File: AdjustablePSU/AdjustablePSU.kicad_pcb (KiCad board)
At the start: 2 copper layers, 99.1 x 96.5 mm, 38 parts

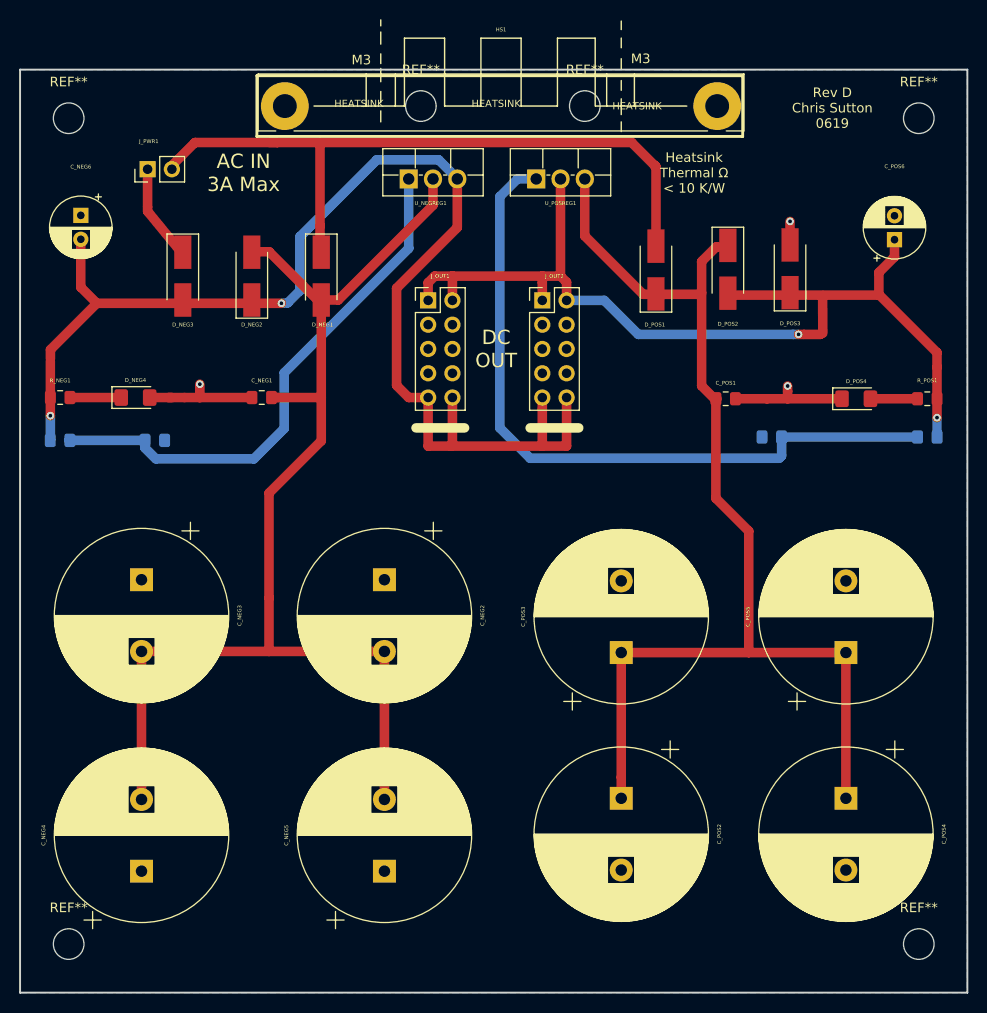
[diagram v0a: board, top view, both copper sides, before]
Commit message: Adjustable PSU RevD
- Layout Redesign 97mm x 50mm
- Removed 4/8 Large Electrolytic Caps
- Added Power Resistor pair to filter ripple.
- Added docs: Layer SVG, Schema SVG/PDF, PNG Renders, STEP 3D model
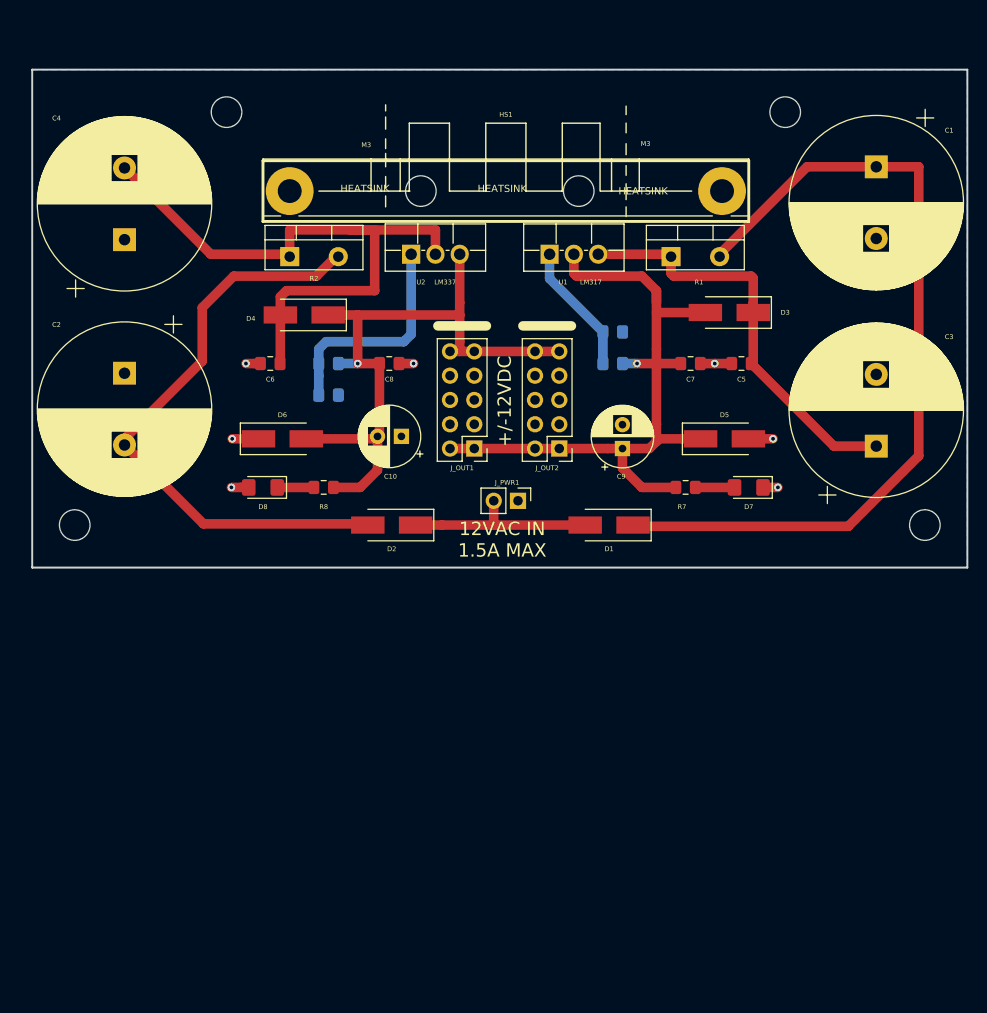
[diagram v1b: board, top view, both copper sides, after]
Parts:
- removed C_NEG1, C_POS1: 100nF, Capacitor_SMD:C_0805_2012Metric_Pad1.15x1.40mm_HandSolder
- removed C_NEG2, C_NEG3, C_NEG4, C_NEG5, C_POS2, C_POS3, C_POS4, C_POS5: 3300uF, Capacitor_THT:CP_Radial_D18.0mm_P7.50mm
- removed C_NEG6, C_POS6: 100uF, Capacitor_THT:CP_Radial_D6.3mm_P2.50mm
- removed D_NEG1, D_NEG2, D_NEG3, D_POS1, D_POS2, D_POS3: HER202G, Diode_SMD:D_SMA_Handsoldering
- removed D_NEG4, D_POS4: LED, LED_SMD:LED_1206_3216Metric_Pad1.42x1.75mm_HandSolder
- removed R_NEG1, R_POS1: 1K, Resistor_SMD:R_0805_2012Metric_Pad1.15x1.40mm_HandSolder
- removed R_NEGREG1, R_POSREG1: 120R, Resistor_SMD:R_0805_2012Metric_Pad1.15x1.40mm_HandSolder
- removed R_NEGREG2, R_POSREG2: 1K1, Resistor_SMD:R_0805_2012Metric_Pad1.15x1.40mm_HandSolder
- removed U_NEGREG1: LM337_TO220, Package_TO_SOT_THT:TO-220F-3_Vertical
- removed U_POSREG1: LM317_3PinPackage, Package_TO_SOT_THT:TO-220F-3_Vertical
- added C1: 3300uF, Capacitor_THT:CP_Radial_D18.0mm_P7.50mm, F.Cu at (188.6, 66.0)
- added C10: 10uF, Capacitor_THT:CP_Radial_D6.3mm_P2.50mm, F.Cu at (138.9, 94.2)
- added C2: 3300uF, Capacitor_THT:CP_Radial_D18.0mm_P7.50mm, F.Cu at (110.0, 87.6)
- added C3: 3300uF, Capacitor_THT:CP_Radial_D18.0mm_P7.50mm, F.Cu at (188.6, 95.2)
- added C4: 3300uF, Capacitor_THT:CP_Radial_D18.0mm_P7.50mm, F.Cu at (110.0, 73.7)
- added C5: 100nF, Capacitor_SMD:C_0805_2012Metric_Pad1.15x1.40mm_HandSolder, F.Cu at (174.5, 86.6)
- added C6: 100nF, Capacitor_SMD:C_0805_2012Metric_Pad1.15x1.40mm_HandSolder, F.Cu at (125.2, 86.6)
- added C7: 100nF, Capacitor_SMD:C_0805_2012Metric_Pad1.15x1.40mm_HandSolder, F.Cu at (169.2, 86.6)
- added C8: 100nF, Capacitor_SMD:C_0805_2012Metric_Pad1.15x1.40mm_HandSolder, F.Cu at (137.7, 86.6)
- added C9: 10uF, Capacitor_THT:CP_Radial_D6.3mm_P2.50mm, F.Cu at (162.1, 95.5)
- added D1: HER202G, Diode_SMD:D_SMA_Handsoldering, F.Cu at (160.7, 103.5)
- added D2: HER202G, Diode_SMD:D_SMA_Handsoldering, F.Cu at (137.9, 103.5)
- added D3: HER202G, Diode_SMD:D_SMA_Handsoldering, F.Cu at (173.2, 81.3)
- added D4: HER202G, Diode_SMD:D_SMA_Handsoldering, F.Cu at (128.8, 81.5)
- added D5: HER202G, Diode_SMD:D_SMA_Handsoldering, F.Cu at (172.7, 94.5)
- added D6: HER202G, Diode_SMD:D_SMA_Handsoldering, F.Cu at (126.5, 94.5)
- added D7: LED, LED_SMD:LED_1206_3216Metric_Pad1.42x1.75mm_HandSolder, F.Cu at (175.3, 99.6)
- added D8: LED, LED_SMD:LED_1206_3216Metric_Pad1.42x1.75mm_HandSolder, F.Cu at (124.5, 99.6)
- added R1: R, Package_TO_SOT_THT:TO-220-2_Vertical, F.Cu at (167.1, 75.4)
- added R2: R, Package_TO_SOT_THT:TO-220-2_Vertical, F.Cu at (127.3, 75.4)
- added R3: 120R, Resistor_SMD:R_0805_2012Metric_Pad1.15x1.40mm_HandSolder, B.Cu at (161.0, 86.6)
- added R4: 1K1, Resistor_SMD:R_0805_2012Metric_Pad1.15x1.40mm_HandSolder, B.Cu at (161.0, 83.3)
- added R5: 120R, Resistor_SMD:R_0805_2012Metric_Pad1.15x1.40mm_HandSolder, B.Cu at (131.3, 86.6)
- added R6: 1K1, Resistor_SMD:R_0805_2012Metric_Pad1.15x1.40mm_HandSolder, B.Cu at (131.3, 89.9)
- added R7: 1K, Resistor_SMD:R_0805_2012Metric_Pad1.15x1.40mm_HandSolder, F.Cu at (168.7, 99.6)
- added R8: 1K, Resistor_SMD:R_0805_2012Metric_Pad1.15x1.40mm_HandSolder, F.Cu at (130.8, 99.6)
- added U1: LM317_3PinPackage, Package_TO_SOT_THT:TO-220F-3_Vertical, F.Cu at (154.4, 75.2)
- added U2: LM337_TO220, Package_TO_SOT_THT:TO-220F-3_Vertical, F.Cu at (140.0, 75.2)
- moved J_PWR1 52.0 mm to (151.1, 101.0), turned to 270 degrees
- moved REF** 43.8 mm to (104.8, 103.5)
- moved REF** 43.8 mm to (193.7, 103.5)
- moved REF** 16.5 mm to (120.7, 60.3)
- moved J_OUT1 16.2 mm to (146.6, 95.5), turned to 180 degrees
- moved J_OUT2 15.6 mm to (155.4, 95.5), turned to 180 degrees
- moved REF** 14.0 mm to (179.1, 60.3)
- moved REF** 8.91 mm to (157.5, 68.6)
- moved HS1 8.90 mm to (149.9, 68.6)
- moved REF** 8.89 mm to (141.0, 68.6)
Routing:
- net Net-(R_POSREG1-Pad2): track 75.8 -> 0.00 mm
- net Net-(C4-Pad2): track 0.00 -> 67.2 mm
- net /12VDC_NEG_REG: track 134.4 -> 69.2 mm, vias 2 -> 1
- net /DC_NEG_IN: track 128.1 -> 64.5 mm
- net Net-(R_NEGREG1-Pad2): track 56.6 -> 0.00 mm
- net /AC_IN: track 74.2 -> 20.3 mm
- net Net-(C3-Pad1): track 0.00 -> 44.8 mm
- net /DC_POS_IN: track 120.9 -> 87.7 mm
- net /12VDC_POS_REG: track 106.0 -> 74.7 mm, vias 2 -> 1
- net Net-(R5-Pad2): track 0.00 -> 23.5 mm
- net GND: track 37.1 -> 15.0 mm, vias 3 -> 7
- net Net-(R3-Pad2): track 0.00 -> 13.7 mm
- net Net-(D_NEG4-Pad1): track 5.11 -> 0.00 mm
- net Net-(D_POS4-Pad2): track 4.57 -> 0.00 mm
- net Net-(D7-Pad2): track 0.00 -> 4.09 mm
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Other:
- board size 99.1 x 96.5 mm -> 97.8 x 52.1 mm
- board text added: "+/-12VDC"
- board text added: "12VAC IN 1.5A MAX"
- board text added: "LM317"
- board text added: "LM337"
- board text added: "RevE 1919 Chris Sutton"
- board text removed: "AC IN 3A Max"
- board text removed: "DC OUT"
- board text removed: "Dual Power Supply"
- board text removed: "Heatsink Thermal Ω < 10 K/W"
- board text removed: "R1"
- board text removed: "R2"
- board text removed: "Rev D Chris Sutton 0619"
- board text removed: "RevB 0219 Chris Sutton"
